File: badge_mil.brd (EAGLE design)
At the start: 77.2 x 83.1 mm, 28 parts, among them U1 TINY2313-*S*, X1 FH12-10S-0.5SH

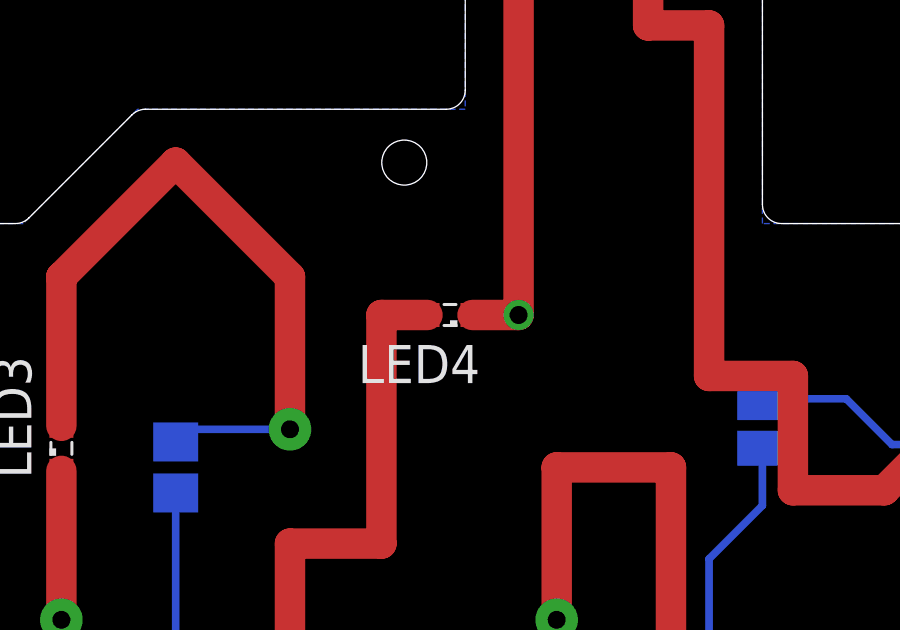
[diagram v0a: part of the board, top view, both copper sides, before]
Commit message: add via like in original logo
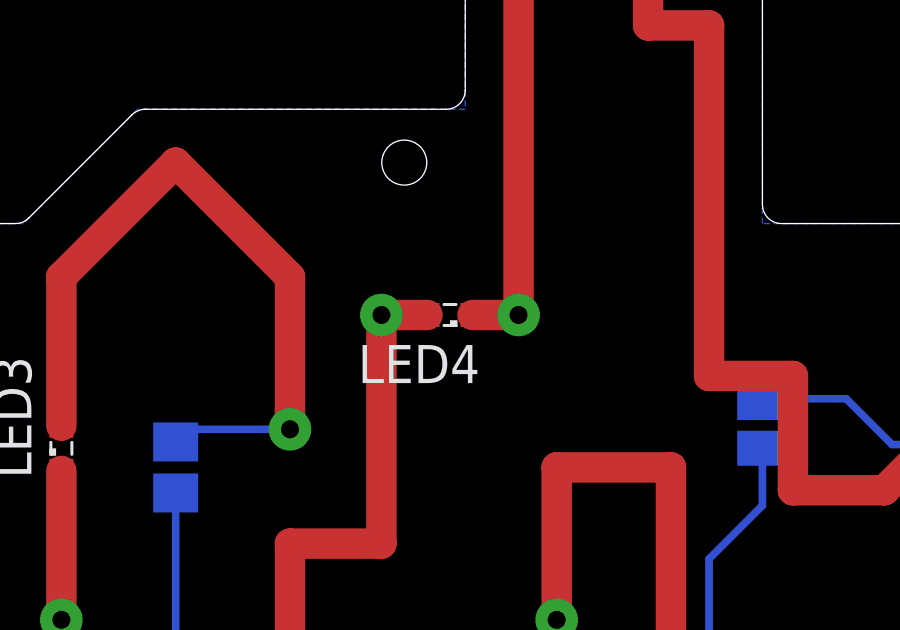
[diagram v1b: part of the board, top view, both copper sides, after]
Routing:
- net N$9: vias 1 -> 2
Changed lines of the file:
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@@
 <layer number="17" name="Pads" color="2" fill="1" visible="yes" active="yes"/>
 <layer number="18" name="Vias" color="2" fill="1" visible="yes" active="yes"/>
-<layer number="19" name="Unrouted" color="6" fill="1" visible="no" active="yes"/>
+<layer number="19" name="Unrouted" color="6" fill="1" visible="yes" active="yes"/>
 <layer number="20" name="Dimension" color="15" fill="1" visible="yes" active="yes"/>
 <layer number="21" name="tPlace" color="7" fill="1" visible="yes" active="yes"/>
-<layer number="22" name="bPlace" color="7" fill="1" visible="no" active="yes"/>
+<layer number="22" name="bPlace" color="7" fill="1" visible="yes" active="yes"/>
 <layer number="23" name="tOrigins" color="15" fill="1" visible="yes" active="yes"/>
-<layer number="24" name="bOrigins" color="15" fill="1" visible="no" active="yes"/>
-<layer number="25" name="tNames" color="7" fill="1" visible="no" active="yes"/>
-<layer number="26" name="bNames" color="7" fill="1" visible="no" active="yes"/>
-<layer number="27" name="tValues" color="7" fill="1" visible="no" active="yes"/>
-<layer number="28" name="bValues" color="7" fill="1" visible="no" active="yes"/>
-<layer number="29" name="tStop" color="7" fill="3" visible="no" active="yes"/>
-<layer number="30" name="bStop" color="7" fill="6" visible="no" active="yes"/>
-<layer number="31" name="tCream" color="7" fill="4" visible="no" active="yes"/>
-<layer number="32" name="bCream" color="7" fill="5" visible="no" active="yes"/>
-<layer number="33" name="tFinish" color="6" fill="3" visible="no" active="yes"/>
-<layer number="34" name="bFinish" color="6" fill="6" visible="no" active="yes"/>
-<layer number="35" name="tGlue" color="7" fill="4" visible="no" active="yes"/>
-<layer number="36" name="bGlue" color="7" fill="5" visible="no" active="yes"/>
-<layer number="37" name="tTest" color="7" fill="1" visible="no" active="yes"/>
-<layer number="38" name="bTest" color="7" fill="1" visible="no" active="yes"/>
-<layer number="39" name="tKeepout" color="4" fill="11" visible="no" active="yes"/>
-<layer number="40" name="bKeepout" color="1" fill="11" visible="no" active="yes"/>
-<layer number="41" name="tRestrict" color="4" fill="10" visible="no" active="yes"/>
-<layer number="42" name="bRestrict" color="1" fill="10" visible="no" active="yes"/>
-<layer number="43" name="vRestrict" color="2" fill="10" visible="no" active="yes"/>
-<layer number="44" name="Drills" color="7" fill="1" visible="no" active="yes"/>
-<layer number="45" name="Holes" color="7" fill="1" visible="no" active="yes"/>
-<layer number="46" name="Milling" color="3" fill="1" visible="no" active="yes"/>
-<layer number="47" name="Measures" color="7" fill="1" visible="no" active="yes"/>
-<layer number="48" name="Document" color="7" fill="1" visible="no" active="yes"/>
-<layer number="49" name="Reference" color="7" fill="1" visible="no" active="yes"/>
+<layer number="24" name="bOrigins" color="15" fill="1" visible="yes" active="yes"/>
+<layer number="25" name="tNames" color="7" fill="1" visible="yes" active="yes"/>
+<layer number="26" name="bNames" color="7" fill="1" visible="yes" active="yes"/>
+<layer number="27" name="tValues" color="7" fill="1" visible="yes" active="yes"/>
+<layer number="28" name="bValues" color="7" fill="1" visible="yes" active="yes"/>
+<layer number="29" name="tStop" color="7" fill="3" visible="yes" active="yes"/>
+<layer number="30" name="bStop" color="7" fill="6" visible="yes" active="yes"/>
+<layer number="31" name="tCream" color="7" fill="4" visible="yes" active="yes"/>
+<layer number="32" name="bCream" color="7" fill="5" visible="yes" active="yes"/>
+<layer number="33" name="tFinish" color="6" fill="3" visible="yes" active="yes"/>
+<layer number="34" name="bFinish" color="6" fill="6" visible="yes" active="yes"/>
+<layer number="35" name="tGlue" color="7" fill="4" visible="yes" active="yes"/>
+<layer number="36" name="bGlue" color="7" fill="5" visible="yes" active="yes"/>
+<layer number="37" name="tTest" color="7" fill="1" visible="yes" active="yes"/>
+<layer number="38" name="bTest" color="7" fill="1" visible="yes" active="yes"/>
+<layer number="39" name="tKeepout" color="4" fill="11" visible="yes" active="yes"/>
+<layer number="40" name="bKeepout" color="1" fill="11" visible="yes" active="yes"/>
+<layer number="41" name="tRestrict" color="4" fill="10" visible="yes" active="yes"/>
+<layer number="42" name="bRestrict" color="1" fill="10" visible="yes" active="yes"/>
+<layer number="43" name="vRestrict" color="2" fill="10" visible="yes" active="yes"/>
+<layer number="44" name="Drills" color="7" fill="1" visible="yes" active="yes"/>
+<layer number="45" name="Holes" color="7" fill="1" visible="yes" active="yes"/>
+<layer number="46" name="Milling" color="3" fill="1" visible="yes" active="yes"/>
+<layer number="47" name="Measures" color="7" fill="1" visible="yes" active="yes"/>
+<layer number="48" name="Document" color="7" fill="1" visible="yes" active="yes"/>
+<layer number="49" name="Reference" color="7" fill="1" visible="yes" active="yes"/>
 <layer number="50" name="dxf" color="7" fill="1" visible="no" active="no"/>
-<layer number="51" name="tDocu" color="7" fill="1" visible="no" active="yes"/>
-<layer number="52" name="bDocu" color="7" fill="1" visible="no" active="yes"/>
+<layer number="51" name="tDocu" color="7" fill="1" visible="yes" active="yes"/>
+<layer number="52" name="bDocu" color="7" fill="1" visible="yes" active="yes"/>
 <layer number="90" name="Modules" color="5" fill="1" visible="no" active="no"/>
 <layer number="91" name="Nets" color="2" fill="1" visible="no" active="no"/>
@@
 <contactref element="LED4" pad="C"/>
 <wire x1="40.882" y1="56.896" x2="42.418" y2="56.896" width="1.016" layer="1"/>
-<via x="42.418" y="56.896" extent="1-16" drill="0.6"/>
+<via x="42.418" y="56.896" extent="1-16" drill="0.6" diameter="1.4224"/>
 <wire x1="43.827" y1="81.28" x2="43.688" y2="81.28" width="1.016" layer="1"/>
 <wire x1="43.688" y1="81.28" x2="43.688" y2="73.152" width="1.016" layer="1"/>
@@
 <wire x1="37.338" y1="26.416" x2="37.973" y2="25.781" width="0.254" layer="16"/>
 <wire x1="37.973" y1="25.781" x2="40.933" y2="25.781" width="0.254" layer="16"/>
+<via x="37.846" y="56.896" extent="1-16" drill="0.6" diameter="1.4224"/>
 </signal>
 <signal name="N$10">

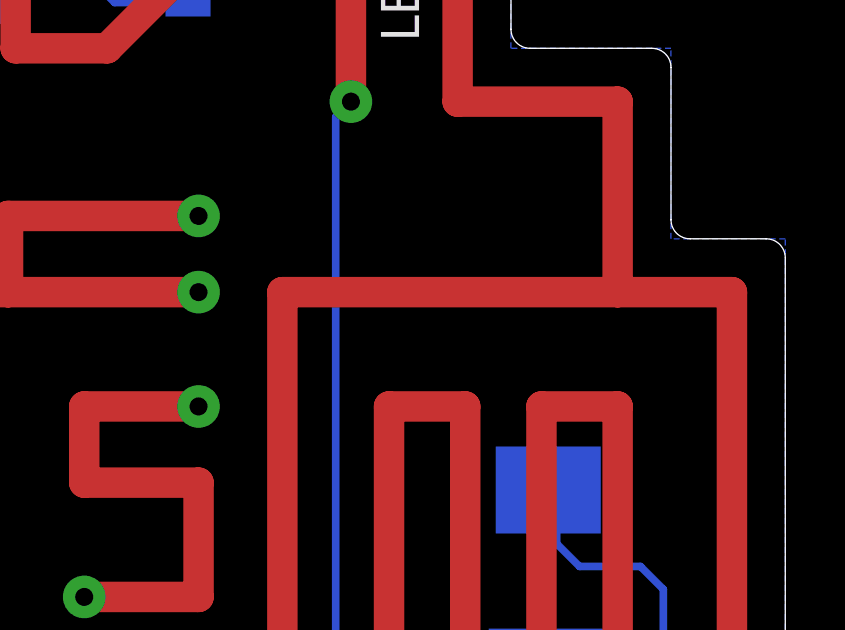
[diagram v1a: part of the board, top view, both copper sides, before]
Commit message: change tStop layer
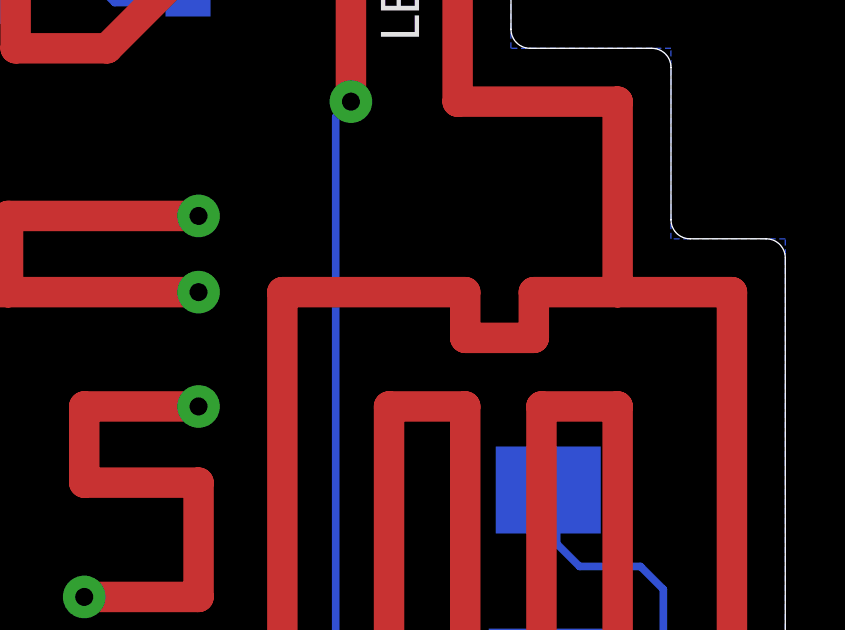
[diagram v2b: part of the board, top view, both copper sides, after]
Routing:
- net GND: track 177.2 -> 180.2 mm
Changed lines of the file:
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@@
 <wire x1="2.54" y1="54.229" x2="2.54" y2="45.339" width="0" layer="20"/>
 <wire x1="2.54" y1="45.339" x2="1.905" y2="44.704" width="0" layer="20" curve="-90"/>
-<polygon width="0" layer="29">
-<vertex x="0" y="24.638"/>
-<vertex x="77.216" y="24.638"/>
-<vertex x="77.216" y="31.75"/>
-<vertex x="77.216" y="83.058"/>
-<vertex x="44.704" y="83.058"/>
-<vertex x="0" y="83.058"/>
-</polygon>
+<wire x1="11.938" y1="26.416" x2="1.778" y2="26.416" width="1.4224" layer="29"/>
+<wire x1="1.778" y1="26.416" x2="1.778" y2="42.926" width="1.4224" layer="29"/>
+<wire x1="1.778" y1="42.926" x2="4.318" y2="42.926" width="1.4224" layer="29"/>
+<wire x1="4.318" y1="42.926" x2="11.938" y2="42.926" width="1.4224" layer="29"/>
+<wire x1="4.318" y1="42.926" x2="4.318" y2="53.086" width="1.4224" layer="29"/>
+<wire x1="4.318" y1="53.086" x2="8.128" y2="53.086" width="1.4224" layer="29"/>
+<wire x1="8.128" y1="53.086" x2="8.128" y2="46.736" width="1.4224" layer="29"/>
+<wire x1="11.938" y1="30.226" x2="5.588" y2="30.226" width="1.4224" layer="29"/>
+<wire x1="5.588" y1="30.226" x2="5.588" y2="39.116" width="1.4224" layer="29"/>
+<wire x1="5.588" y1="39.116" x2="11.938" y2="39.116" width="1.4224" layer="29"/>
+<wire x1="24.638" y1="26.416" x2="14.478" y2="26.416" width="1.4224" layer="29"/>
+<wire x1="14.478" y1="26.416" x2="14.478" y2="42.926" width="1.4224" layer="29"/>
+<wire x1="14.478" y1="42.926" x2="22.098" y2="42.926" width="1.4224" layer="29"/>
+<wire x1="22.098" y1="42.926" x2="22.098" y2="49.276" width="1.4224" layer="29"/>
+<wire x1="22.098" y1="49.276" x2="19.558" y2="49.276" width="1.4224" layer="29"/>
+<wire x1="19.558" y1="49.276" x2="10.668" y2="49.276" width="1.4224" layer="29"/>
+<wire x1="19.558" y1="49.276" x2="19.558" y2="58.166" width="1.4224" layer="29"/>
+<wire x1="19.558" y1="58.166" x2="15.748" y2="58.166" width="1.4224" layer="29"/>
+<wire x1="15.748" y1="58.166" x2="15.748" y2="53.086" width="1.4224" layer="29"/>
+<wire x1="24.638" y1="30.226" x2="18.288" y2="30.226" width="1.4224" layer="29"/>
+<wire x1="18.288" y1="30.226" x2="18.288" y2="39.116" width="1.4224" layer="29"/>
+<wire x1="18.288" y1="39.116" x2="24.638" y2="39.116" width="1.4224" layer="29"/>
+<wire x1="27.178" y1="46.736" x2="27.178" y2="58.166" width="1.4224" layer="29"/>
+<wire x1="27.178" y1="58.166" x2="30.988" y2="61.976" width="1.4224" layer="29"/>
+<wire x1="30.988" y1="61.976" x2="34.798" y2="58.166" width="1.4224" layer="29"/>
+<wire x1="34.798" y1="58.166" x2="34.798" y2="53.086" width="1.4224" layer="29"/>
+<wire x1="37.338" y1="26.416" x2="27.178" y2="26.416" width="1.4224" layer="29"/>
+<wire x1="27.178" y1="26.416" x2="27.178" y2="42.926" width="1.4224" layer="29"/>
+<wire x1="27.178" y1="42.926" x2="34.798" y2="42.926" width="1.4224" layer="29"/>
+<wire x1="34.798" y1="42.926" x2="34.798" y2="49.276" width="1.4224" layer="29"/>
+<wire x1="34.798" y1="49.276" x2="37.846" y2="49.276" width="1.4224" layer="29"/>
+<wire x1="37.846" y1="49.276" x2="37.846" y2="56.896" width="1.4224" layer="29"/>
+<wire x1="37.846" y1="56.896" x2="42.418" y2="56.896" width="1.4224" layer="29"/>
+<wire x1="42.418" y1="56.896" x2="42.418" y2="73.152" width="1.4224" layer="29"/>
+<wire x1="42.418" y1="73.152" x2="43.688" y2="73.152" width="1.4224" layer="29"/>
+<wire x1="43.688" y1="73.152" x2="43.688" y2="81.28" width="1.4224" layer="29"/>
+<wire x1="43.688" y1="81.28" x2="45.466" y2="81.28" width="1.4224" layer="29"/>
+<wire x1="45.466" y1="81.28" x2="45.466" y2="70.612" width="1.4224" layer="29"/>
+<wire x1="45.466" y1="70.612" x2="46.736" y2="70.612" width="1.4224" layer="29"/>
+<wire x1="46.736" y1="70.612" x2="46.736" y2="66.548" width="1.4224" layer="29"/>
+<wire x1="46.736" y1="66.548" x2="48.768" y2="66.548" width="1.4224" layer="29"/>
+<wire x1="48.768" y1="66.548" x2="48.768" y2="54.864" width="1.4224" layer="29"/>
+<wire x1="48.768" y1="54.864" x2="51.562" y2="54.864" width="1.4224" layer="29"/>
+<wire x1="51.562" y1="54.864" x2="51.562" y2="51.054" width="1.4224" layer="29"/>
+<wire x1="51.562" y1="51.054" x2="54.61" y2="51.054" width="1.4224" layer="29"/>
+<wire x1="54.61" y1="51.054" x2="59.69" y2="56.134" width="1.4224" layer="29"/>
+<wire x1="43.688" y1="30.226" x2="43.688" y2="26.416" width="1.4224" layer="29"/>
+<wire x1="43.688" y1="26.416" x2="39.878" y2="26.416" width="1.4224" layer="29"/>
+<wire x1="39.878" y1="26.416" x2="39.878" y2="42.926" width="1.4224" layer="29"/>
+<wire x1="39.878" y1="42.926" x2="47.498" y2="42.926" width="1.4224" layer="29"/>
+<wire x1="47.498" y1="42.926" x2="47.498" y2="51.816" width="1.4224" layer="29"/>
+<wire x1="47.498" y1="51.816" x2="43.688" y2="51.816" width="1.4224" layer="29"/>
+<wire x1="43.688" y1="51.816" x2="43.688" y2="46.736" width="1.4224" layer="29"/>
+<wire x1="37.338" y1="30.226" x2="30.988" y2="30.226" width="1.4224" layer="29"/>
+<wire x1="30.988" y1="30.226" x2="30.988" y2="39.116" width="1.4224" layer="29"/>
+<wire x1="30.988" y1="39.116" x2="37.338" y2="39.116" width="1.4224" layer="29"/>
+<wire x1="43.688" y1="32.766" x2="47.498" y2="32.766" width="1.4224" layer="29"/>
+<wire x1="47.498" y1="32.766" x2="47.498" y2="36.576" width="1.4224" layer="29"/>
+<wire x1="47.498" y1="36.576" x2="43.688" y2="36.576" width="1.4224" layer="29"/>
+<wire x1="43.688" y1="36.576" x2="43.688" y2="39.116" width="1.4224" layer="29"/>
+<wire x1="43.688" y1="39.116" x2="47.498" y2="39.116" width="1.4224" layer="29"/>
+<wire x1="53.848" y1="30.226" x2="53.848" y2="26.416" width="1.4224" layer="29"/>
+<wire x1="53.848" y1="26.416" x2="50.038" y2="26.416" width="1.4224" layer="29"/>
+<wire x1="50.038" y1="26.416" x2="50.038" y2="42.926" width="1.4224" layer="29"/>
+<wire x1="50.038" y1="42.926" x2="51.308" y2="42.926" width="1.4224" layer="29"/>
+<wire x1="51.308" y1="42.926" x2="57.658" y2="42.926" width="1.4224" layer="29"/>
+<wire x1="57.658" y1="45.466" x2="51.308" y2="45.466" width="1.4224" layer="29"/>
+<wire x1="51.308" y1="45.466" x2="51.308" y2="42.926" width="1.4224" layer="29"/>
+<wire x1="53.848" y1="32.766" x2="57.658" y2="32.766" width="1.4224" layer="29"/>
+<wire x1="57.658" y1="32.766" x2="57.658" y2="36.576" width="1.4224" layer="29"/>
+<wire x1="57.658" y1="36.576" x2="53.848" y2="36.576" width="1.4224" layer="29"/>
+<wire x1="53.848" y1="36.576" x2="53.848" y2="39.116" width="1.4224" layer="29"/>
+<wire x1="53.848" y1="39.116" x2="57.658" y2="39.116" width="1.4224" layer="29"/>
+<wire x1="60.452" y1="26.416" x2="60.452" y2="42.926" width="1.4224" layer="29"/>
+<wire x1="60.452" y1="42.926" x2="66.548" y2="42.926" width="1.4224" layer="29"/>
+<wire x1="66.548" y1="42.926" x2="66.548" y2="41.402" width="1.4224" layer="29"/>
+<wire x1="66.548" y1="41.402" x2="68.834" y2="41.402" width="1.4224" layer="29"/>
+<wire x1="68.834" y1="41.402" x2="68.834" y2="42.926" width="1.4224" layer="29"/>
+<wire x1="68.834" y1="42.926" x2="71.628" y2="42.926" width="1.4224" layer="29"/>
+<wire x1="71.628" y1="42.926" x2="75.438" y2="42.926" width="1.4224" layer="29"/>
+<wire x1="75.438" y1="42.926" x2="75.438" y2="26.416" width="1.4224" layer="29"/>
+<wire x1="71.628" y1="26.416" x2="71.628" y2="39.116" width="1.4224" layer="29"/>
+<wire x1="71.628" y1="39.116" x2="69.088" y2="39.116" width="1.4224" layer="29"/>
+<wire x1="69.088" y1="39.116" x2="69.088" y2="26.416" width="1.4224" layer="29"/>
+<wire x1="66.548" y1="26.416" x2="66.548" y2="39.116" width="1.4224" layer="29"/>
+<wire x1="66.548" y1="39.116" x2="64.008" y2="39.116" width="1.4224" layer="29"/>
+<wire x1="64.008" y1="39.116" x2="64.008" y2="26.416" width="1.4224" layer="29"/>
+<wire x1="62.738" y1="49.276" x2="62.738" y2="58.166" width="1.4224" layer="29"/>
+<wire x1="62.738" y1="58.166" x2="66.294" y2="58.166" width="1.4224" layer="29"/>
+<wire x1="66.294" y1="58.166" x2="66.294" y2="49.276" width="1.4224" layer="29"/>
+<wire x1="66.294" y1="49.276" x2="71.628" y2="49.276" width="1.4224" layer="29"/>
+<wire x1="71.628" y1="49.276" x2="71.628" y2="42.926" width="1.4224" layer="29"/>
 </plain>
 <attributes>
@@
 <wire x1="66.294" y1="49.276" x2="71.628" y2="49.276" width="1.016" layer="1"/>
 <wire x1="71.628" y1="49.276" x2="71.628" y2="42.926" width="1.016" layer="1"/>
-<wire x1="71.628" y1="42.926" x2="60.452" y2="42.926" width="1.016" layer="1"/>
+<wire x1="71.628" y1="42.926" x2="68.834" y2="42.926" width="1.016" layer="1"/>
+<wire x1="68.834" y1="42.926" x2="68.834" y2="41.402" width="1.016" layer="1"/>
+<wire x1="68.834" y1="41.402" x2="66.548" y2="41.402" width="1.016" layer="1"/>
+<wire x1="66.548" y1="41.402" x2="66.548" y2="42.926" width="1.016" layer="1"/>
+<wire x1="66.548" y1="42.926" x2="60.452" y2="42.926" width="1.016" layer="1"/>
 <wire x1="60.452" y1="42.926" x2="60.452" y2="26.416" width="1.016" layer="1"/>
 <wire x1="71.628" y1="42.926" x2="75.438" y2="42.926" width="1.016" layer="1"/>

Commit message: Resistor Package
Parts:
- R3: device resistor:R0603 -> resistor:R0805
- SJ1: device jumper:SJ -> jumper:SJW
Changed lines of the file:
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@@
 <?xml version="1.0" encoding="utf-8"?>
 <!DOCTYPE eagle SYSTEM "eagle.dtd">
-<eagle version="7.2.0">
+<eagle version="7.1.0">
 <drawing>
 <settings>
@@
 <attribute name="SPICEPREFIX" value="R" x="6.223" y="21.971" size="1.778" layer="28" rot="MR0" display="off"/>
 </element>
-<element name="R3" library="resistor" package="R0603" value="" x="12.446" y="35.814" rot="MR90">
+<element name="R3" library="resistor" package="R0805" value="" x="12.446" y="35.814" rot="MR90">
 <attribute name="SPICEPREFIX" value="R" x="12.446" y="35.814" size="1.778" layer="28" rot="MR90" display="off"/>
 </element>
@@
 <attribute name="SPICEPREFIX" value="R" x="57.308" y="53.616" size="1.778" layer="28" rot="MR90" display="off"/>
 </element>
-<element name="SJ1" library="jumper" package="SJ" value="" x="50.508" y="53.216" rot="MR270"/>
+<element name="SJ1" library="jumper" package="SJW" value="" x="50.508" y="53.216" rot="MR270"/>
 </elements>
 <signals>
@@
 <wire x1="48.768" y1="48.768" x2="50.546" y2="50.546" width="0.254" layer="16"/>
 <wire x1="50.546" y1="50.546" x2="50.546" y2="52.324" width="0.254" layer="16"/>
-<wire x1="50.546" y1="52.324" x2="50.508" y2="52.454" width="0.254" layer="16"/>
+<wire x1="50.546" y1="52.324" x2="50.508" y2="51.946" width="0.254" layer="16"/>
 </signal>
 <signal name="N$4">
@@
 <contactref element="R8" pad="1"/>
 <contactref element="SJ1" pad="1"/>
-<wire x1="50.508" y1="53.978" x2="50.508" y2="54.064" width="0.254" layer="16"/>
+<wire x1="50.508" y1="54.486" x2="50.508" y2="54.064" width="0.254" layer="16"/>
 <wire x1="50.508" y1="54.064" x2="50.546" y2="54.102" width="0.254" layer="16"/>
 <wire x1="50.546" y1="54.102" x2="53.34" y2="54.102" width="0.254" layer="16"/>
